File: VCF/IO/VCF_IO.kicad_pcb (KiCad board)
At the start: 2 copper layers, 39.6 x 111.8 mm, 14 parts, among them J1 Res Mod, J2 Cutoff Mod, J3 In1, J4 In2, J5 In3, J6 Out, J7 IO

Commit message: Clean up VCF boards
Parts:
- added REF**: OSHW-Logo2_7.3x6mm_SilkScreen, Symbol:OSHW-Logo2_7.3x6mm_SilkScreen, B.Cu at (75.2, 52.8)
- J7: moved to B.Cu
- turned J7 to 180 degrees
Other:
- board text added: "+12V"
- board text added: "-12V"
- board text added: "Cutoff"
- board text added: "Cutoff Amt"
- board text added: "Cutoff Mod"
- board text added: "CutoffM"
- board text added: "In 1"
- board text added: "In 1 Amt"
- board text added: "In 2"
- board text added: "In 2 Amt"
- board text added: "In 3"
- board text added: "In 3 Amt"
- board text added: "In_1"
- board text added: "In_2"
- board text added: "In_3"
- board text added: "Out"
- board text added: "Res"
- board text added: "Res Amt"
- board text added: "Res Mod"
- board text added: "ResM"
- board text added: "Resonance"
- board text added: "VCF IO Board Rev 1"
- board text added: "WH"

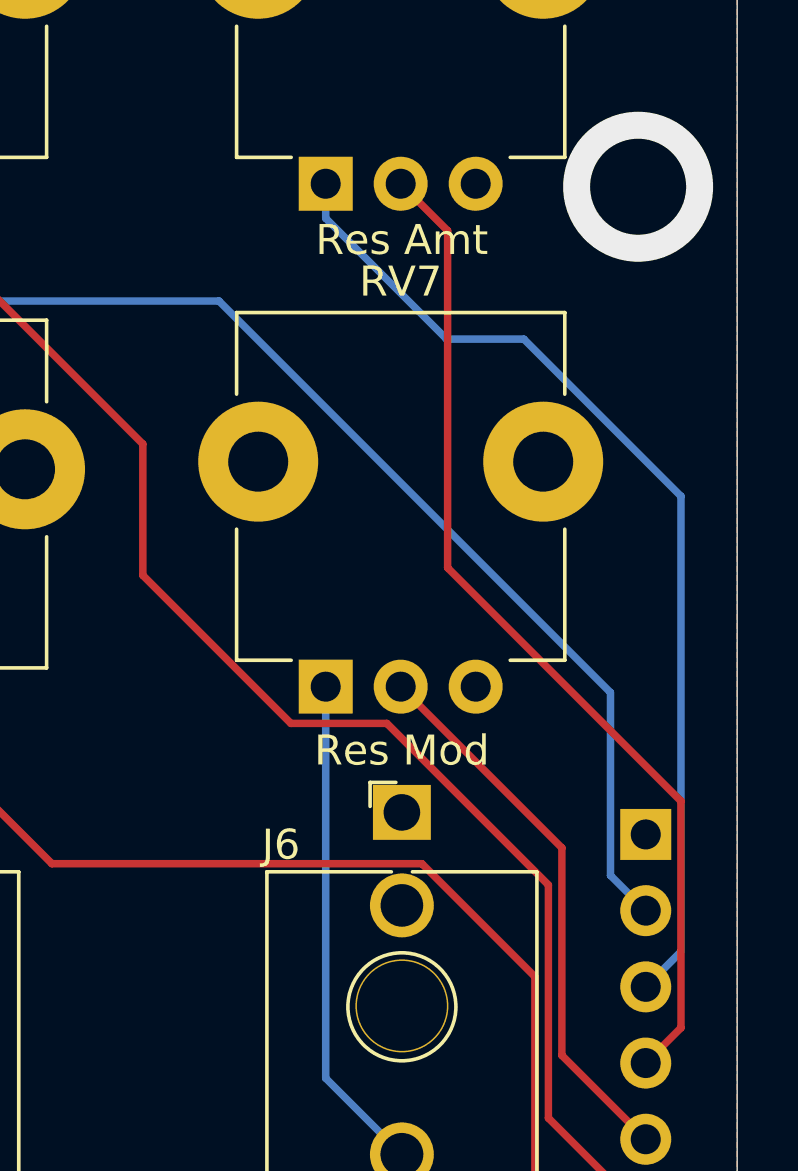
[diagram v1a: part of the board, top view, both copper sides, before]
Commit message: Fix inverted resonance control input
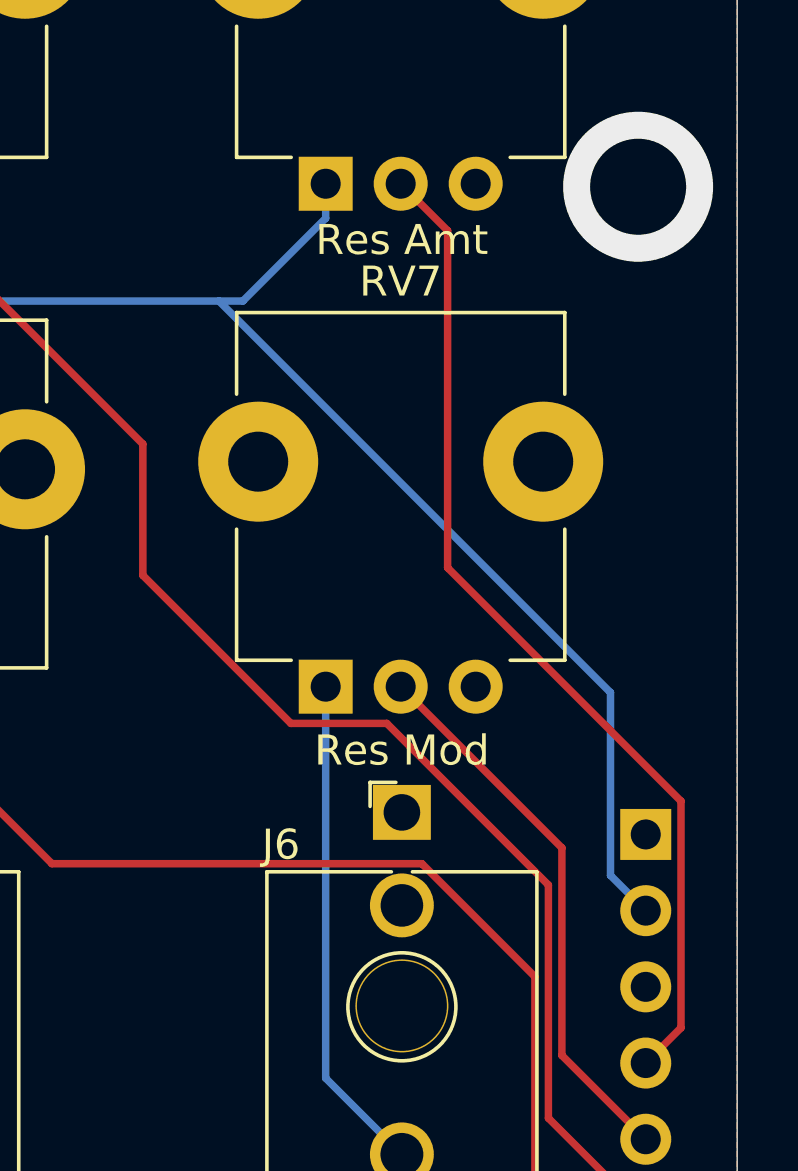
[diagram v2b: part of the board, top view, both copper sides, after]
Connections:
- RV6 pad 1: -12V -> +12V
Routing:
- net -12V: track 33.7 -> 0.00 mm
- net +12V: track 42.2 -> 48.1 mm
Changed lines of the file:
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@@
     (thickness 1.6)
     (drawings 29)
-    (tracks 76)
+    (tracks 73)
     (zones 0)
     (modules 15)
@@
     (mod_text_size 1 1)
     (mod_text_width 0.15)
-    (pad_size 4 4)
-    (pad_drill 2)
+    (pad_size 1.8 1.8)
+    (pad_drill 1)
     (pad_to_mask_clearance 0.051)
     (solder_mask_min_width 0.25)
@@
       (net 11 /Res))
     (pad 1 thru_hole rect (at -2.54 7.52) (size 1.8 1.8) (drill 1) (layers *.Cu *.Mask)
-      (net 10 -12V))
+      (net 9 +12V))
     (model ${KISYS3DMOD}/Potentiometer_THT.3dshapes/Potentiometer_TT_P0915N.wrl
       (at (xyz 0 0 0))
@@
   (segment (start 75.404 71.12) (end 72.644 68.36) (width 0.25) (layer B.Cu) (net 9))
   (segment (start 86.36 71.12) (end 75.404 71.12) (width 0.25) (layer B.Cu) (net 9))
-  (segment (start 100.584 93.98) (end 101.759001 92.804999) (width 0.25) (layer B.Cu) (net 10))
-  (segment (start 101.759001 77.625999) (end 96.523002 72.39) (width 0.25) (layer B.Cu) (net 10))
-  (segment (start 101.759001 92.804999) (end 101.759001 77.625999) (width 0.25) (layer B.Cu) (net 10))
-  (segment (start 89.916 68.36) (end 89.916 67.21) (width 0.25) (layer B.Cu) (net 10))
-  (segment (start 93.946 72.39) (end 89.916 68.36) (width 0.25) (layer B.Cu) (net 10))
-  (segment (start 96.523002 72.39) (end 93.946 72.39) (width 0.25) (layer B.Cu) (net 10))
+  (segment (start 89.916 68.36) (end 87.156 71.12) (width 0.25) (layer B.Cu) (net 9))
+  (segment (start 87.156 71.12) (end 86.36 71.12) (width 0.25) (layer B.Cu) (net 9))
+  (segment (start 89.916 67.21) (end 89.916 68.36) (width 0.25) (layer B.Cu) (net 9))
   (segment (start 101.759001 95.344999) (end 101.759001 87.789001) (width 0.25) (layer F.Cu) (net 11))
   (segment (start 100.584 96.52) (end 101.759001 95.344999) (width 0.25) (layer F.Cu) (net 11))

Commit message: Bunch of bug fixes and tweaks
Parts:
- added H1: Top_MH1, Eurorack:eurorack_mounting_hole, F.Cu at (67.3, 67.3)
- added H2: Bottom_MH1, Eurorack:eurorack_mounting_hole, F.Cu at (67.3, 135.9)
- added H3: Top_MH2, Eurorack:eurorack_mounting_hole, F.Cu at (100.3, 67.3)
- added H4: Bottom_MH2, Eurorack:eurorack_mounting_hole, F.Cu at (100.3, 135.9)
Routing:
- net GNDREF: vias 4 -> 0
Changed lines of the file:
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@@
-(kicad_pcb (version 20171130) (host pcbnew 5.1.4)
+(kicad_pcb (version 20171130) (host pcbnew "(5.1.4-0-10_14)")
   (general
     (thickness 1.6)
     (drawings 29)
-    (tracks 73)
+    (tracks 69)
     (zones 0)
-    (modules 15)
+    (modules 19)
     (nets 18)
   )
@@
     (mod_text_size 1 1)
     (mod_text_width 0.15)
-    (pad_size 1.8 1.8)
-    (pad_drill 1)
+    (pad_size 4 4)
+    (pad_drill 2)
     (pad_to_mask_clearance 0.051)
     (solder_mask_min_width 0.25)
@@
       (outputformat 1)
       (mirror false)
-      (drillshape 1)
+      (drillshape 0)
       (scaleselection 1)
-      (outputdirectory ""))
+      (outputdirectory "Gerbers"))
   )
   (net 0 "")
@@
     )
   )
+  (module Eurorack:eurorack_mounting_hole (layer F.Cu)
+    (at 67.31 67.31)
+    (fp_text reference H1 (at 0 0.5) (layer F.SilkS) hide
+      (effects (font (size 1 1) (thickness 0.15)))
+    )
+    (fp_text value Top_MH1 (at 0 -0.5) (layer F.Fab) hide
+      (effects (font (size 1 1) (thickness 0.15)))
+    )
+    (pad 1 thru_hole circle (at 0 0) (size 5 5) (drill 3.2) (layers *.Cu *.Mask)
+      (net 7 GNDREF))
+  )
+  (module Eurorack:eurorack_mounting_hole (layer F.Cu)
+    (at 67.31 135.89)
+    (fp_text reference H2 (at 0 0.5) (layer F.SilkS) hide
+      (effects (font (size 1 1) (thickness 0.15)))
+    )
+    (fp_text value Bottom_MH1 (at 0 -0.5) (layer F.Fab) hide
+      (effects (font (size 1 1) (thickness 0.15)))
+    )
+    (pad 1 thru_hole circle (at 0 0) (size 5 5) (drill 3.2) (layers *.Cu *.Mask)
+      (net 7 GNDREF))
+  )
+  (module Eurorack:eurorack_mounting_hole (layer F.Cu)
+    (at 100.33 67.31)
+    (fp_text reference H3 (at 0 0.5) (layer F.SilkS) hide
+      (effects (font (size 1 1) (thickness 0.15)))
+    )
+    (fp_text value Top_MH2 (at 0 -0.5) (layer F.Fab) hide
+      (effects (font (size 1 1) (thickness 0.15)))
+    )
+    (pad 1 thru_hole circle (at 0 0) (size 5 5) (drill 3.2) (layers *.Cu *.Mask)
+      (net 7 GNDREF))
+  )
+  (module Eurorack:eurorack_mounting_hole (layer F.Cu)
+    (at 100.33 135.89)
+    (fp_text reference H4 (at 0 0.5) (layer F.SilkS) hide
+      (effects (font (size 1 1) (thickness 0.15)))
+    )
+    (fp_text value Bottom_MH2 (at 0 -0.5) (layer F.Fab) hide
+      (effects (font (size 1 1) (thickness 0.15)))
+    )
+    (pad 1 thru_hole circle (at 0 0) (size 5 5) (drill 3.2) (layers *.Cu *.Mask)
+      (net 7 GNDREF))
+  )
   (gr_text Out (at 84.836 152.146) (layer F.SilkS)
     (effects (font (size 1 1) (thickness 0.15)))
@@
   (segment (start 89.916 97.025) (end 92.456 99.565) (width 0.25) (layer B.Cu) (net 6))
   (segment (start 89.916 83.974) (end 89.916 97.025) (width 0.25) (layer B.Cu) (net 6))
-  (via (at 67.31 135.89) (size 4.99999) (drill 3.2004) (layers F.Cu B.Cu) (net 7))
-  (via (at 100.33 135.89) (size 4.99999) (drill 3.2004) (layers F.Cu B.Cu) (net 7))
-  (via (at 100.33 67.31) (size 4.99999) (drill 3.2004) (layers F.Cu B.Cu) (net 7))
-  (via (at 67.31 67.31) (size 4.99999) (drill 3.2004) (layers F.Cu B.Cu) (net 7))
   (segment (start 96.39 118.494) (end 96.39 154.94) (width 0.25) (layer F.Cu) (net 8))
   (segment (start 100.584 114.3) (end 96.39 118.494) (width 0.25) (layer F.Cu) (net 8))

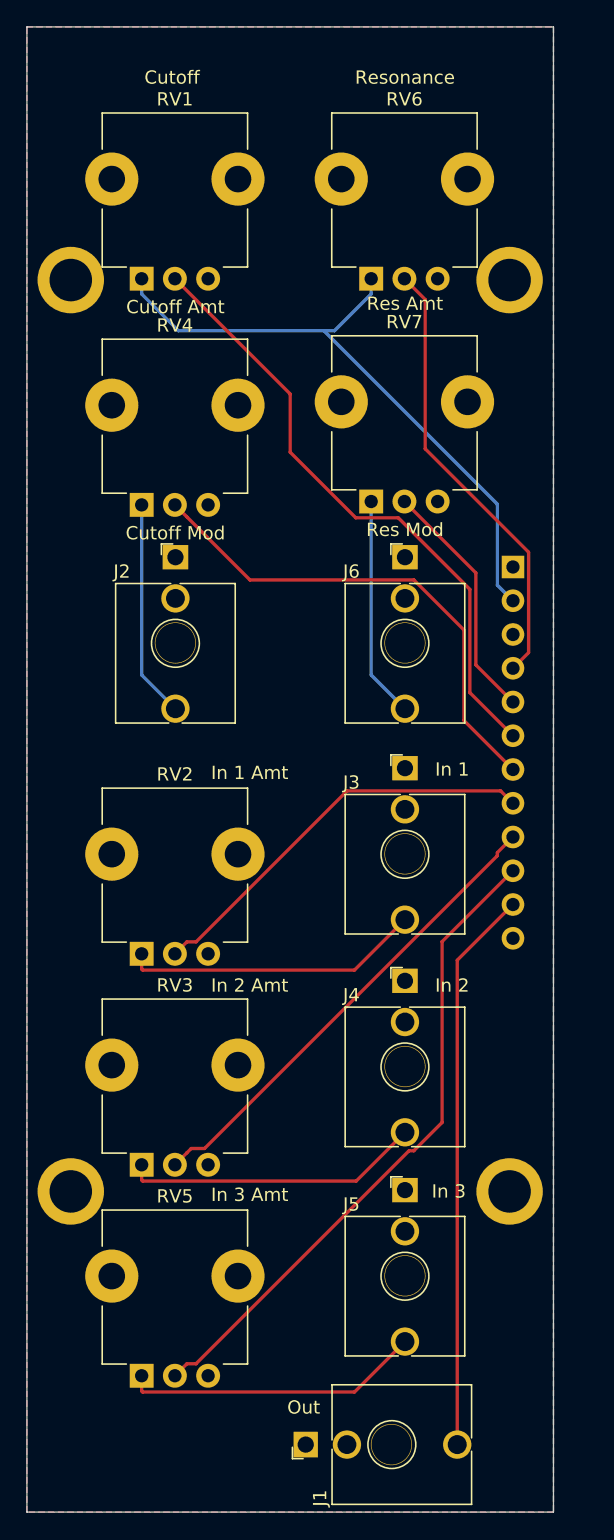
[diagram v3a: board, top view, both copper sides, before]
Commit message: Make VCF front panel bigger. Re-align IO and FP boards.
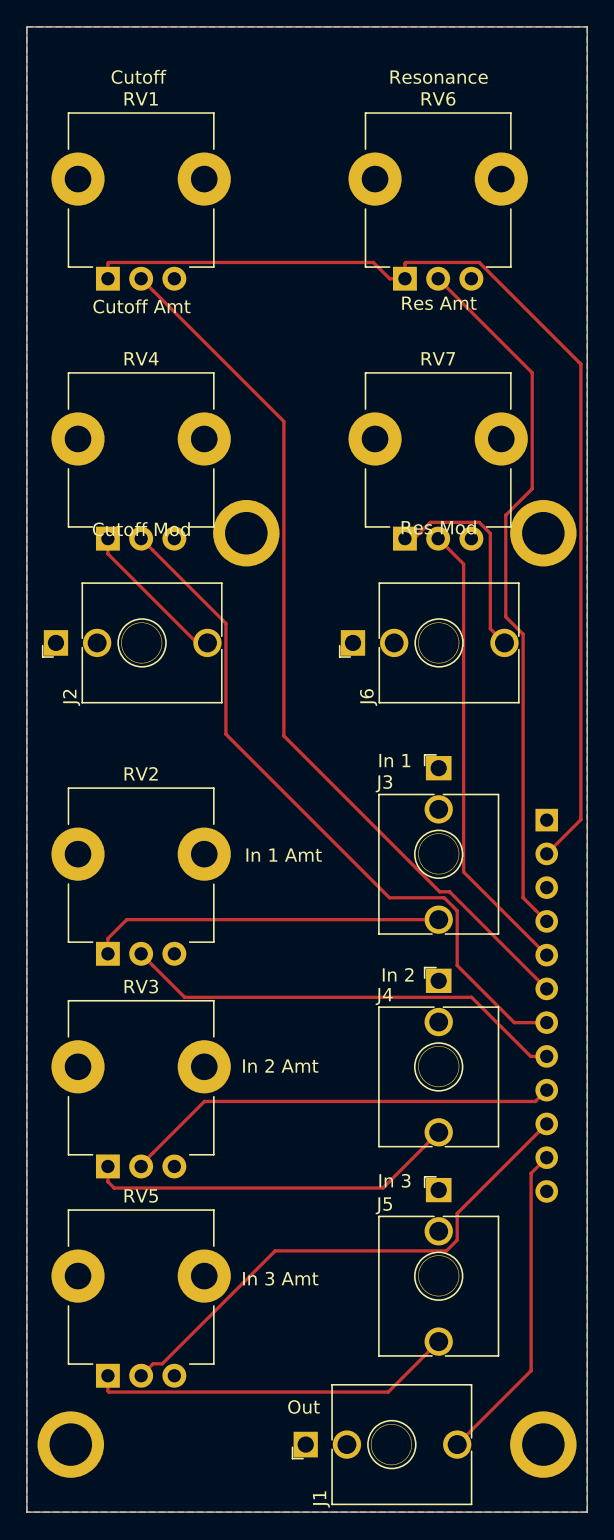
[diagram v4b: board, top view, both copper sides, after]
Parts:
- moved H1 23.2 mm to (80.5, 86.4)
- moved H4 19.2 mm to (102.9, 154.9)
- moved H2 19.2 mm to (69.8, 154.9)
- moved H3 19.2 mm to (102.9, 86.4)
- moved J7 19.2 mm to (103.1, 108.0)
- moved REF** 3.94 mm to (79.0, 51.8)
- moved RV7 3.78 mm to (95.0, 79.2)
- moved RV4 3.59 mm to (72.6, 79.2)
- moved RV3 2.54 mm to (72.6, 126.5)
- moved J2 2.54 mm to (72.6, 94.6), turned to 90 degrees
- moved J3 2.54 mm to (95.0, 110.5)
- moved J4 2.54 mm to (95.0, 126.5)
- moved J5 2.54 mm to (95.0, 142.2)
- moved J6 2.54 mm to (95.0, 94.6), turned to 90 degrees
- moved RV1 2.54 mm to (72.6, 59.7)
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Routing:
- net +12V: track 48.1 -> 79.5 mm
- net /Res: track 33.7 -> 53.4 mm
- net /Cutoff: track 46.8 -> 66.5 mm
- net /Out: track 42.4 -> 24.4 mm
- net /Res_Mod: track 18.5 -> 34.7 mm
- net /Cutoff_Mod: track 37.7 -> 52.9 mm
- net /In_3: track 49.2 -> 39.5 mm
- net Net-(J4-PadT): track 22.5 -> 28.7 mm
- net Net-(J5-PadT): track 22.6 -> 27.6 mm
- net Net-(J2-PadT): track 16.4 -> 11.4 mm
- net Net-(J3-PadT): track 22.6 -> 26.6 mm
- net /In_2: track 35.8 -> 32.8 mm
- net /In_1: track 30.9 -> 33.7 mm
- net Net-(J6-PadT): track 16.6 -> 16.0 mm
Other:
- board size 39.6 x 111.8 mm -> 42.2 x 111.8 mm

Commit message: Fix backwards knobs
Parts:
- removed REF**: OSHW-Logo2_7.3x6mm_SilkScreen, Symbol:OSHW-Logo2_7.3x6mm_SilkScreen
- J1: value Res Mod -> Out
- J6: value Out -> Res Mod
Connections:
- RV1 pad 1: +12V -> GNDREF
- RV1 pad 3: GNDREF -> +12V
- RV2 pad 1: Net-(J3-PadT) -> GNDREF
- RV2 pad 3: GNDREF -> Net-(J3-PadT)
- RV3 pad 1: Net-(J4-PadT) -> GNDREF
- RV3 pad 3: GNDREF -> Net-(J4-PadT)
- RV4 pad 1: Net-(J2-PadT) -> GNDREF
- RV4 pad 3: GNDREF -> Net-(J2-PadT)
- RV5 pad 1: Net-(J5-PadT) -> GNDREF
- RV5 pad 3: GNDREF -> Net-(J5-PadT)
- RV6 pad 1: +12V -> GNDREF
- RV6 pad 3: GNDREF -> +12V
- RV7 pad 1: Net-(J6-PadT) -> GNDREF
- RV7 pad 3: GNDREF -> Net-(J6-PadT)
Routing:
- net Net-(J4-PadT): track 28.7 -> 21.0 mm
- net +12V: track 79.5 -> 72.2 mm
- net Net-(J6-PadT): track 16.0 -> 8.88 mm
- net Net-(J5-PadT): track 27.6 -> 21.0 mm
- net Net-(J3-PadT): track 26.6 -> 21.0 mm
- net Net-(J2-PadT): track 11.4 -> 9.67 mm
